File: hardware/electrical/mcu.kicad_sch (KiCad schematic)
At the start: 40 parts, among them J1 STDC14, SW1 SW_Push, U1 STM32F446ZET6, U2 SRV05-4, Y1 X322516MLB4SI

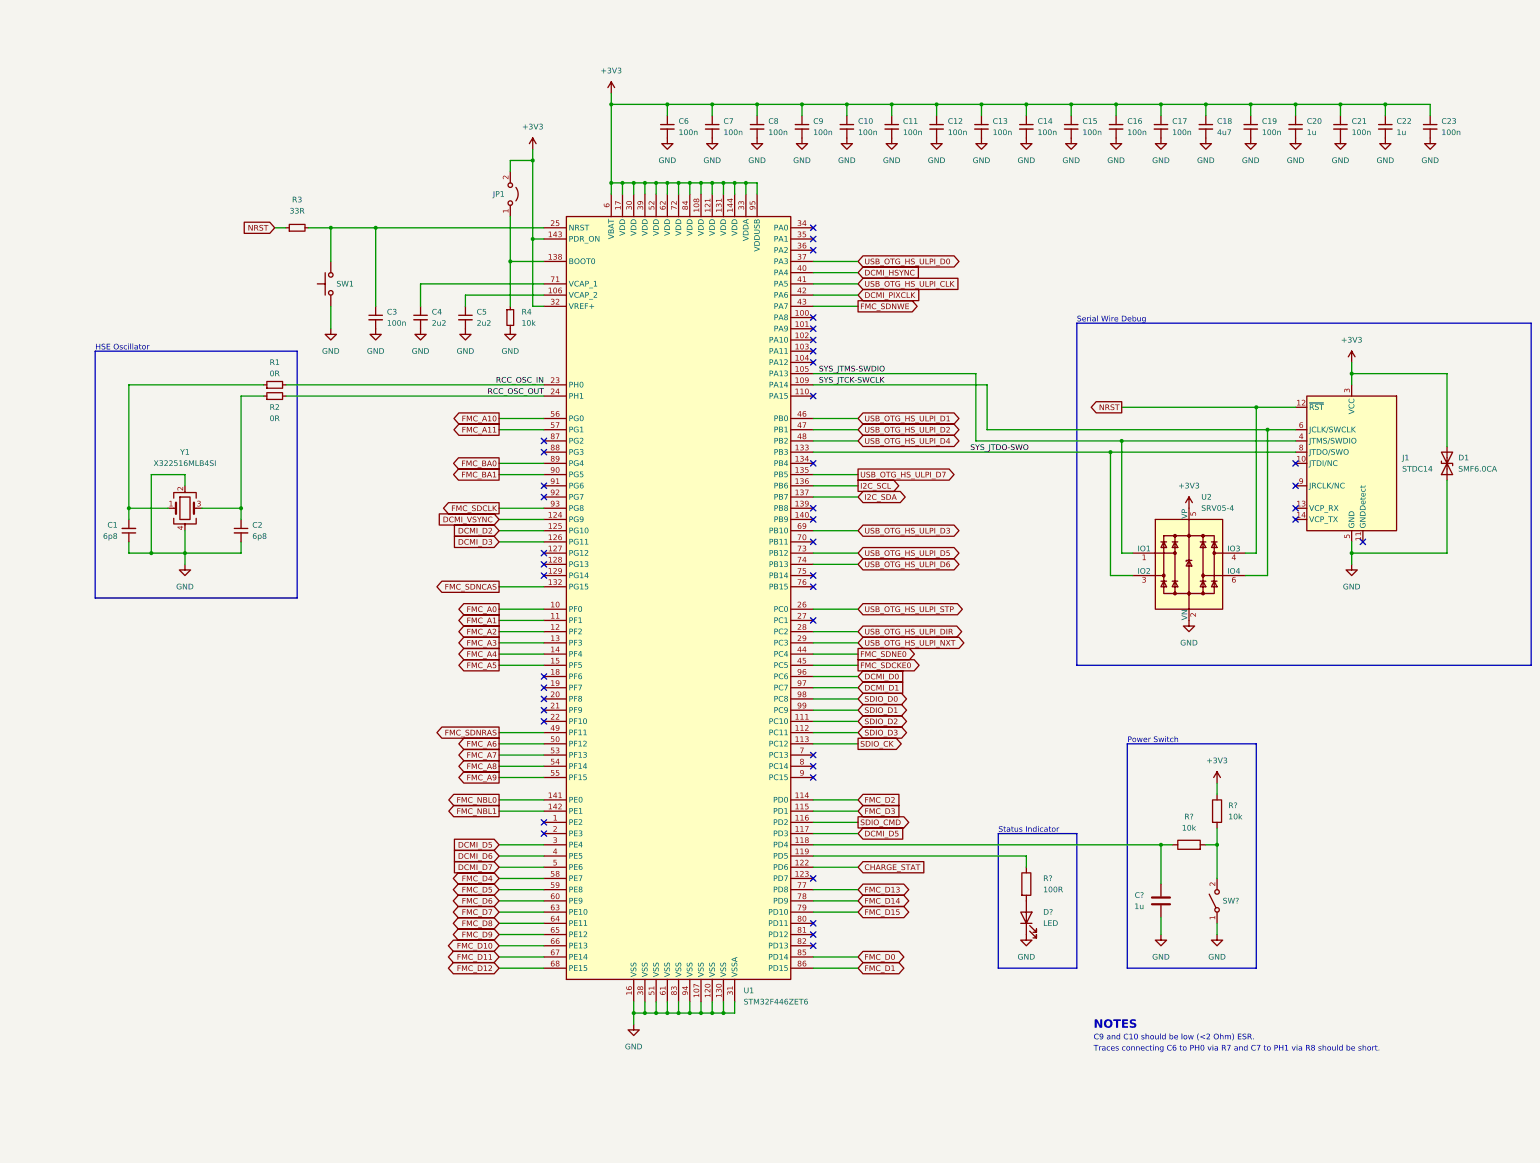
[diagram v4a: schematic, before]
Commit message: Add LSE oscillator
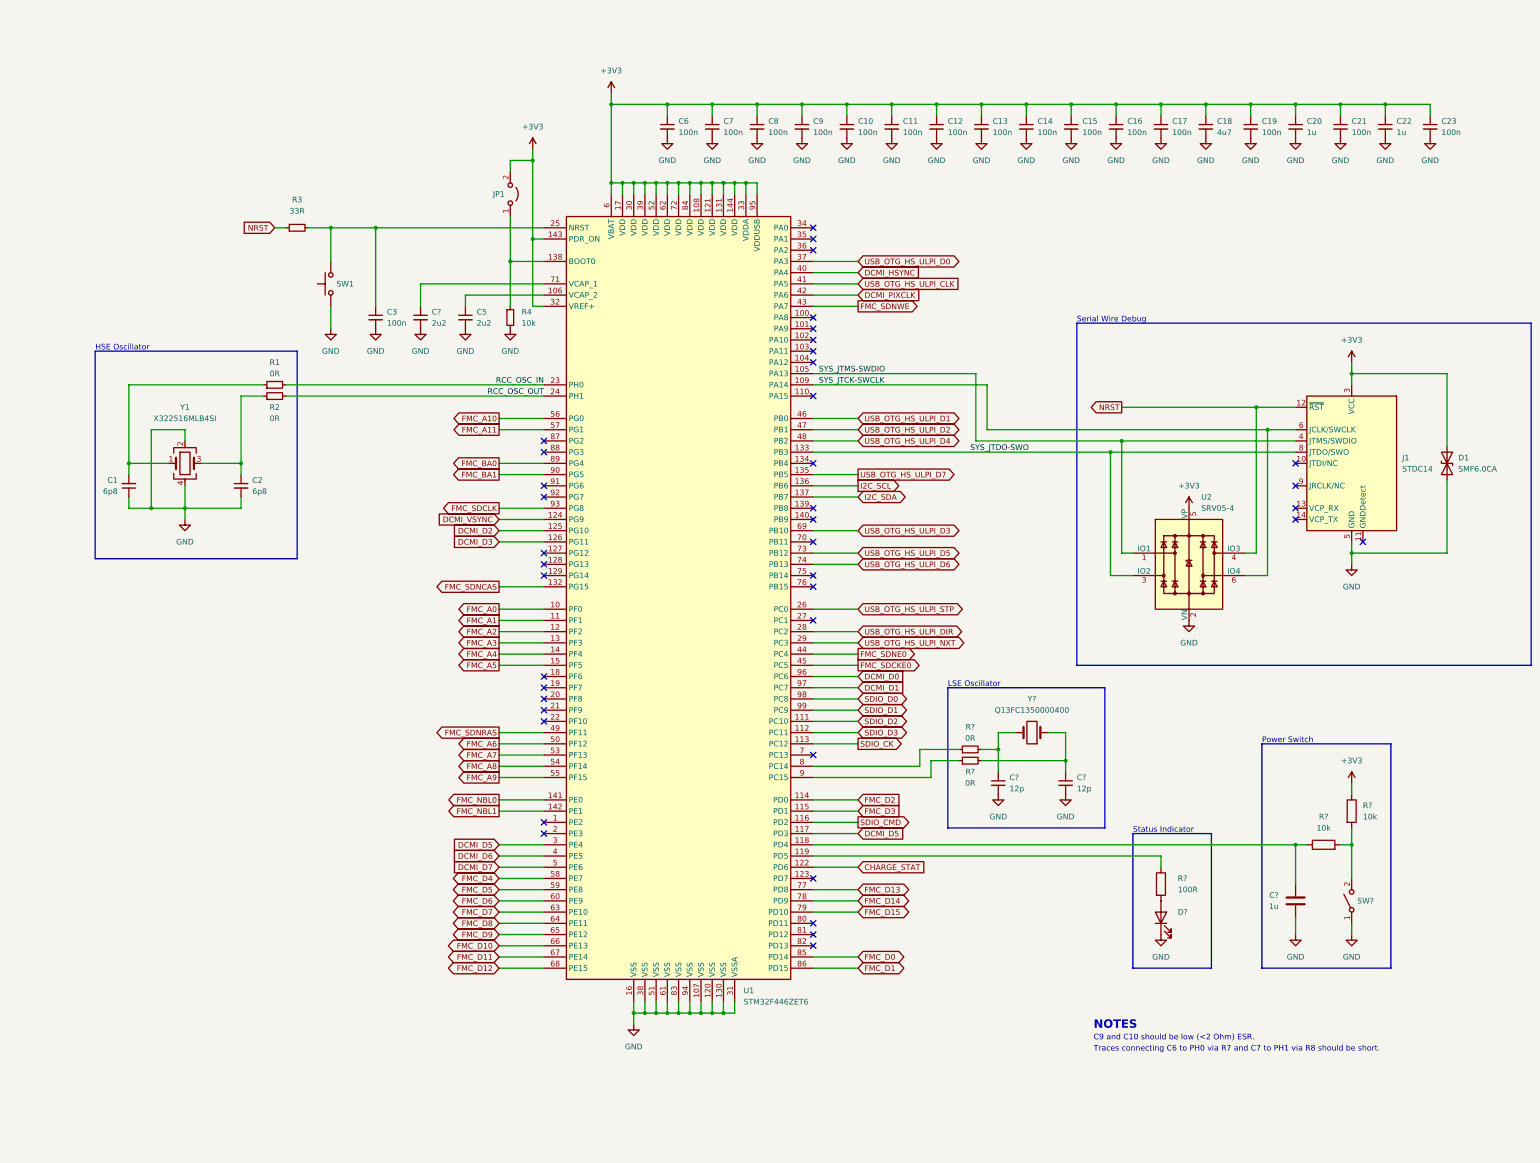
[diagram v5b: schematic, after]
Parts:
- added C? (x2): 12p, symbol Device:C_Small
- added R? (x2): 0R, symbol Device:R_Small
- added Y?: Q13FC1350000400, symbol Device:Crystal
- D?: value LED -> (none)
- renumbered C4 to C?
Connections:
- net GND: now also C?.2, C?.2
- net at U1.8 (PC14): now also R?.1
- net at U1.9 (PC15): now also R?.1
- new net: C?.1, R?.2, Y?.2
- new net: C?.1, R?.2, Y?.1
- no-connect marks 42 -> 40
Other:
- note added: "LSE Oscillator"
- moved on the sheet: C1, C2, C?, D?, R?, SW?, Y1

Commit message: Move power switch to WKUP0 pin and make it positive logic
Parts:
- D?: value (none) -> LED
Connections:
- net +3V3: now also SW?.2 (B); no longer R?.1
- net GND: now also R?.2; no longer SW?.1 (A)
- net SYS_WKUP0: now reaches C?.2, R?.1
- net SYS_WKUP0: now also U1.34 (PA0); no longer U1.118 (PD4)
- new net: R?.1, R?.2, SW?.1 (A)
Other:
- moved on the sheet: C?, D?, R?, SW?

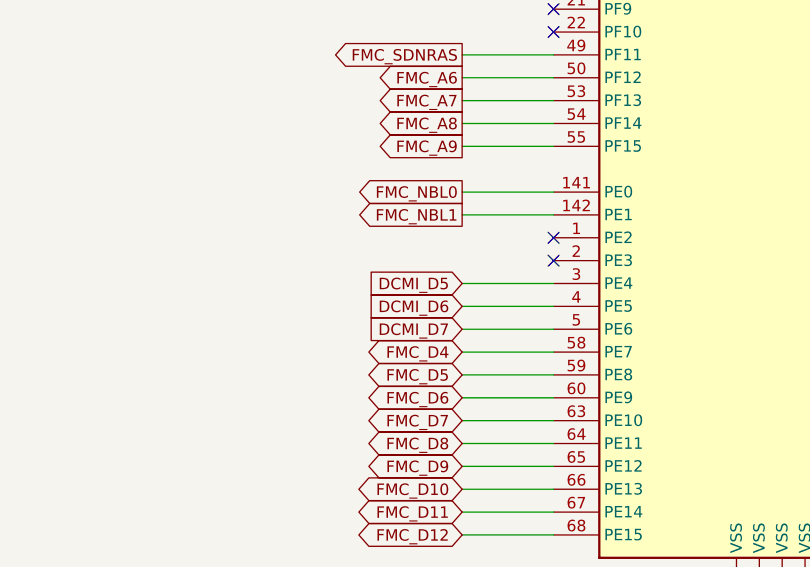
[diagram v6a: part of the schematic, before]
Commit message: Fix typo - PE4 should be DCMI_D4
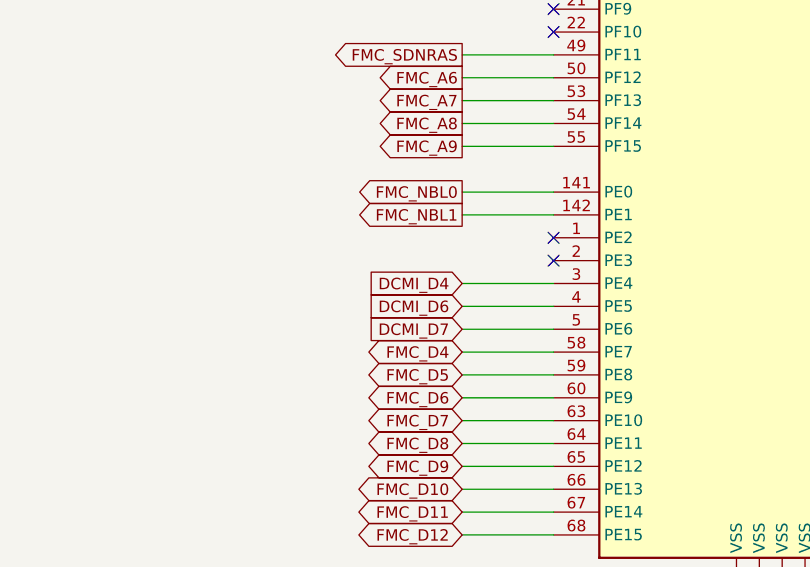
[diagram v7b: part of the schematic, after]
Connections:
- net DCMI_D5: no longer U1.3 (PE4)
- new net DCMI_D4: U1.3 (PE4)
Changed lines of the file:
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@@
     )
   )
-  (global_label "DCMI_D5" (shape input) (at 165.1 205.74 180) (fields_autoplaced)
+  (global_label "DCMI_D4" (shape input) (at 165.1 205.74 180) (fields_autoplaced)
     (effects (font (size 1.27 1.27)) (justify right))
     (property "Intersheet References" "${INTERSHEET_REFS}" (id 0) (at 154.6436 205.6606 0)

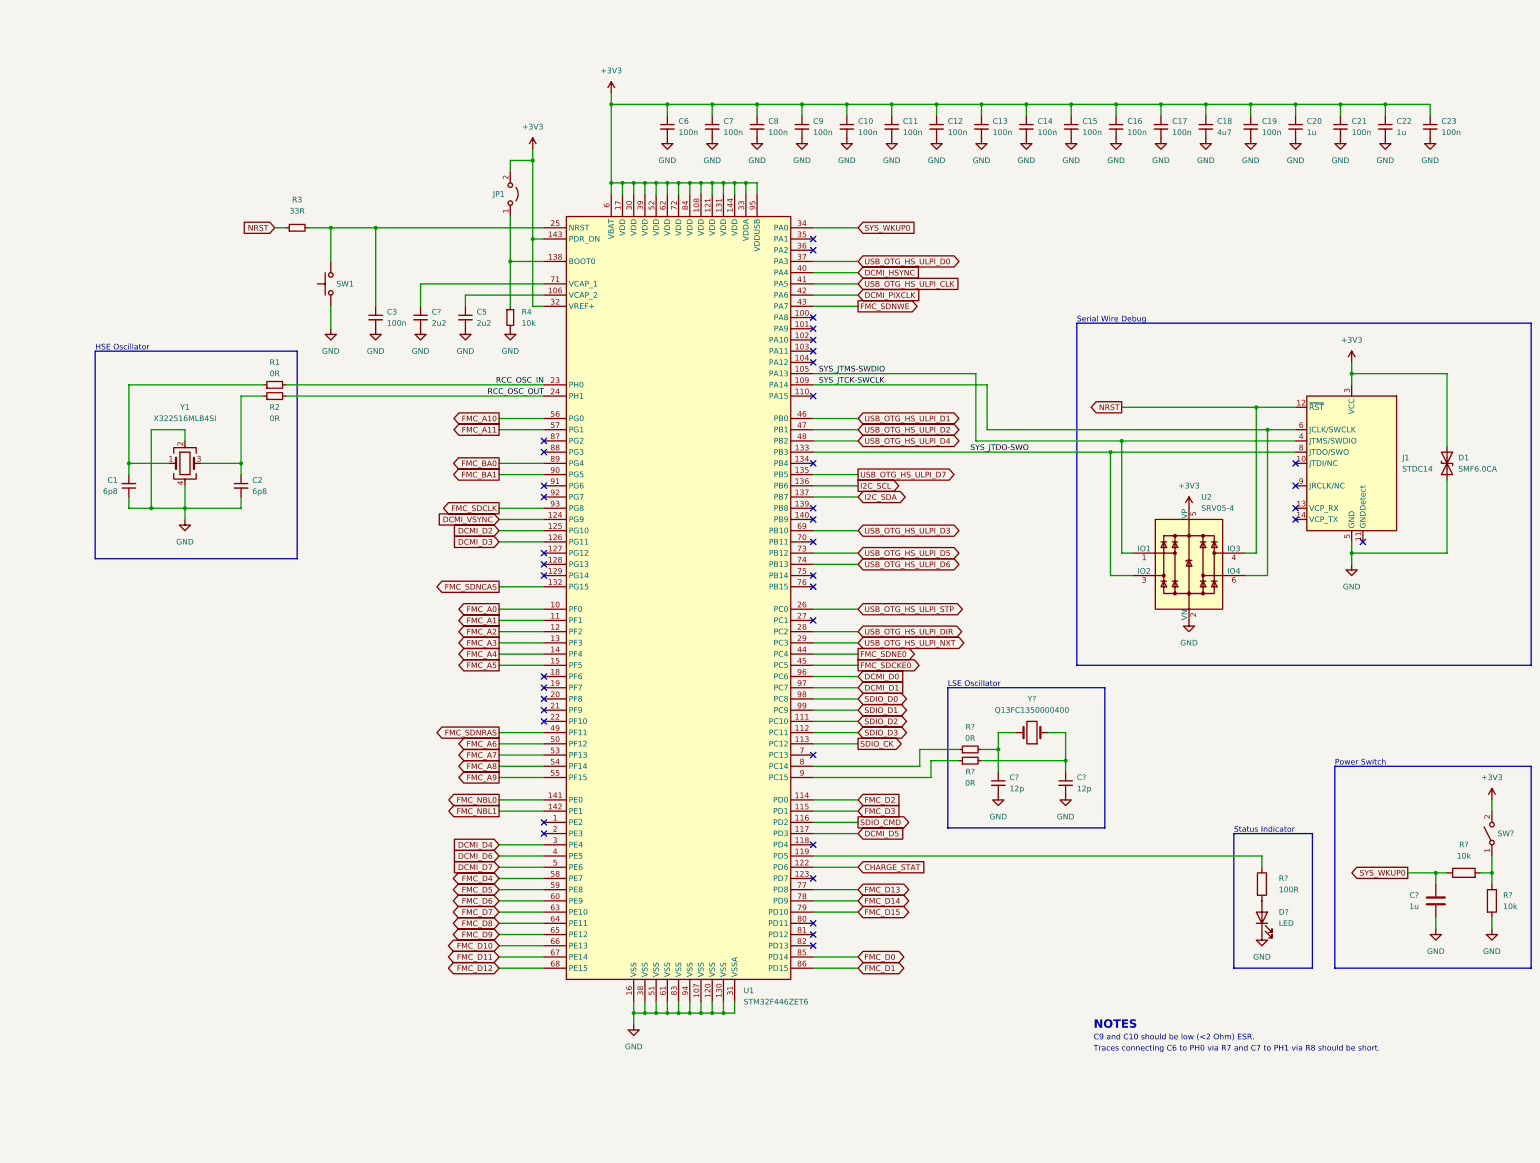
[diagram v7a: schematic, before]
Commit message: Add VDD cutoff circuitry
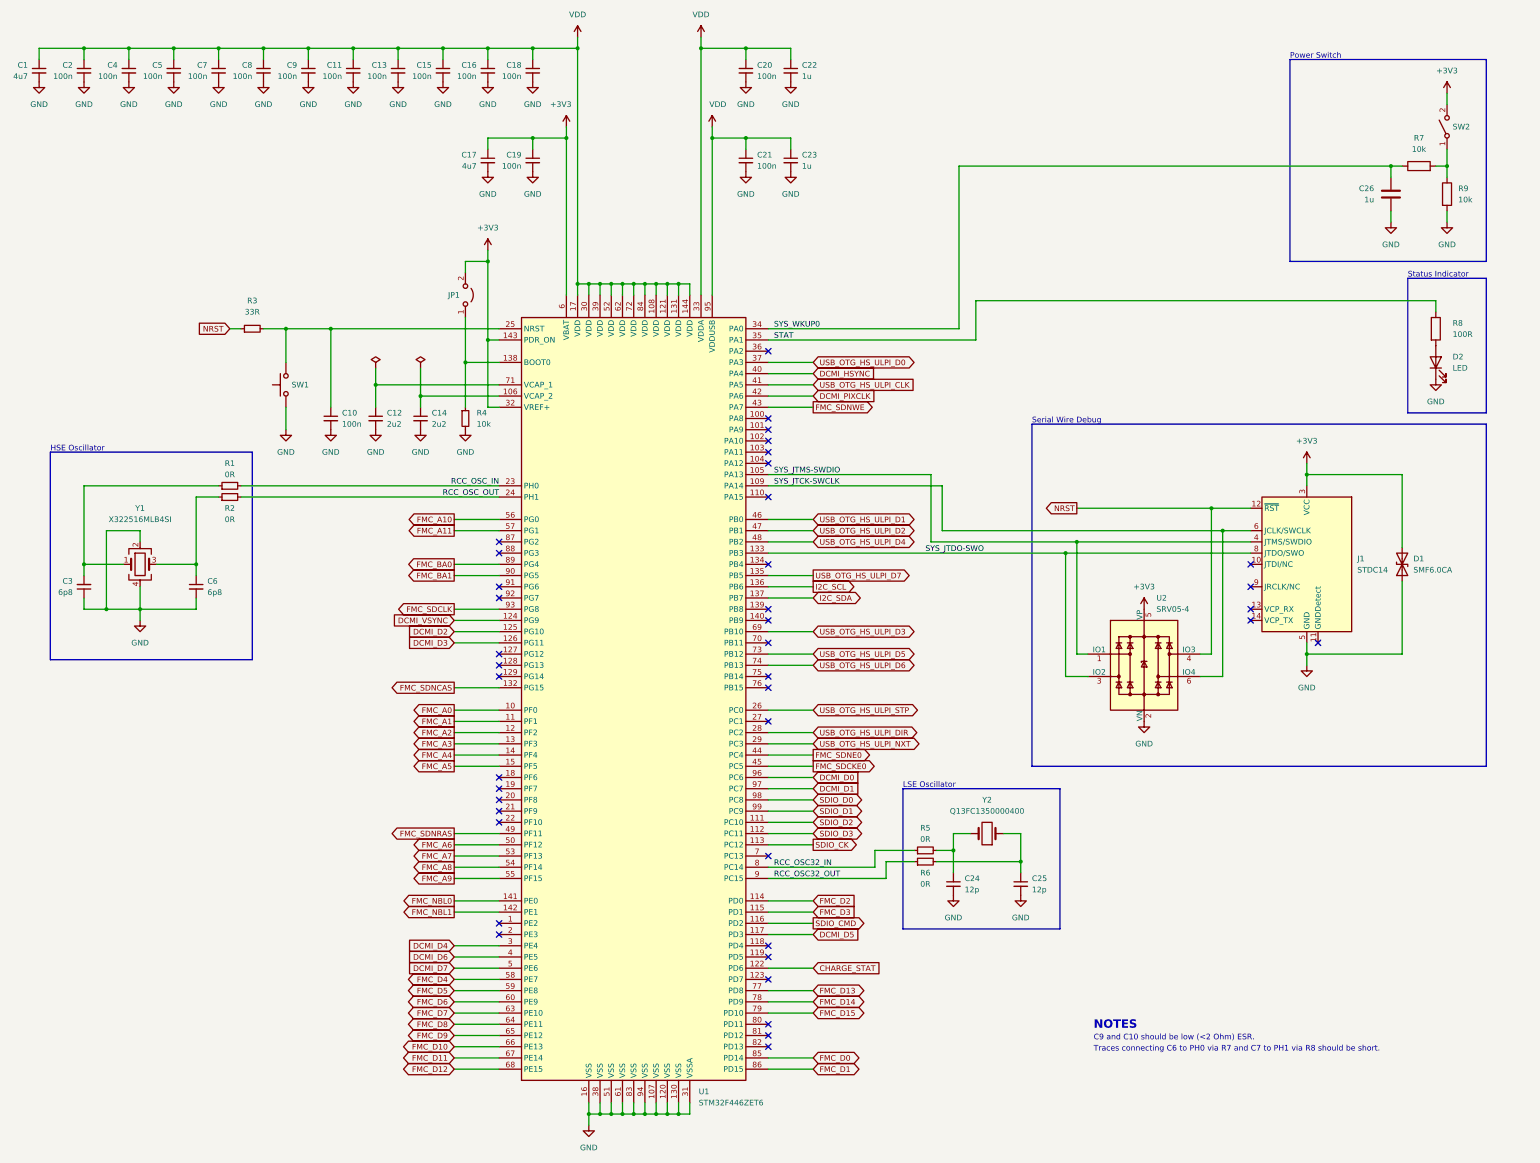
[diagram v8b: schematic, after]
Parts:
- removed C22: 1u, symbol Device:C_Small
- added C19: 100n, symbol Device:C_Small
- C17: value 100n -> 4u7
- C23: value 100n -> 1u
- gave numbers to parts that had none: 12
- renumbered C18 to C1, C3 to C10, C10 to C11, C9 to C13, C5 to C14, C8 to C15, C7 to C16, C6 to C18, C16 to C2, C19 to C20, C20 to C22, C1 to C3, C15 to C4, C14 to C5, C2 to C6, C13 to C7, C12 to C8, C11 to C9
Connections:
- net +3V3: now also C19.1; no longer C1.1, C11.1, C13.1, C15.1, C16.1, C18.1, C2.1, C20.1, C21.1, C22.1, C23.1, C4.1, C5.1, C7.1, C8.1, C9.1, U1.108 (VDD), U1.121 (VDD), U1.131 (VDD), U1.144 (VDD), U1.17 (VDD), U1.30 (VDD), U1.33 (VDDA), U1.39 (VDD), U1.52 (VDD), U1.62 (VDD), U1.72 (VDD), U1.84 (VDD), U1.95 (VDDUSB)
- net GND: now also C19.2
- net RCC_OSC32_IN: now reaches R5.1, U1.8 (PC14)
- net at U1.119 (PD5): no longer R8.1
- net RCC_OSC32_OUT: now reaches R6.1, U1.9 (PC15)
- net STAT: now reaches U1.35 (PA1)
- net STAT: now also R8.1
- new net VDD: C1.1, C11.1, C13.1, C15.1, C16.1, C18.1, C2.1, C20.1, C21.1, C22.1, C23.1, C4.1, C5.1, C7.1, C8.1, C9.1, U1.108 (VDD), U1.121 (VDD), U1.131 (VDD), U1.144 (VDD), U1.17 (VDD), U1.30 (VDD), U1.33 (VDDA), U1.39 (VDD), U1.52 (VDD), U1.62 (VDD), U1.72 (VDD), U1.84 (VDD), U1.95 (VDDUSB)
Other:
- moved on the sheet: C1, C10, C11, C12, C13, C14, C15, C16, C18, C2, C20, C22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
